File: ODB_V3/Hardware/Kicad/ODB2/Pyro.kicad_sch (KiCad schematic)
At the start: 51 parts, among them J1 Screw_Terminal_01x08, U11 SI5442DU-T1-GE3, U12 SI5442DU-T1-GE3, U2 LM339, U3 SI5442DU-T1-GE3, U8 SI5442DU-T1-GE3

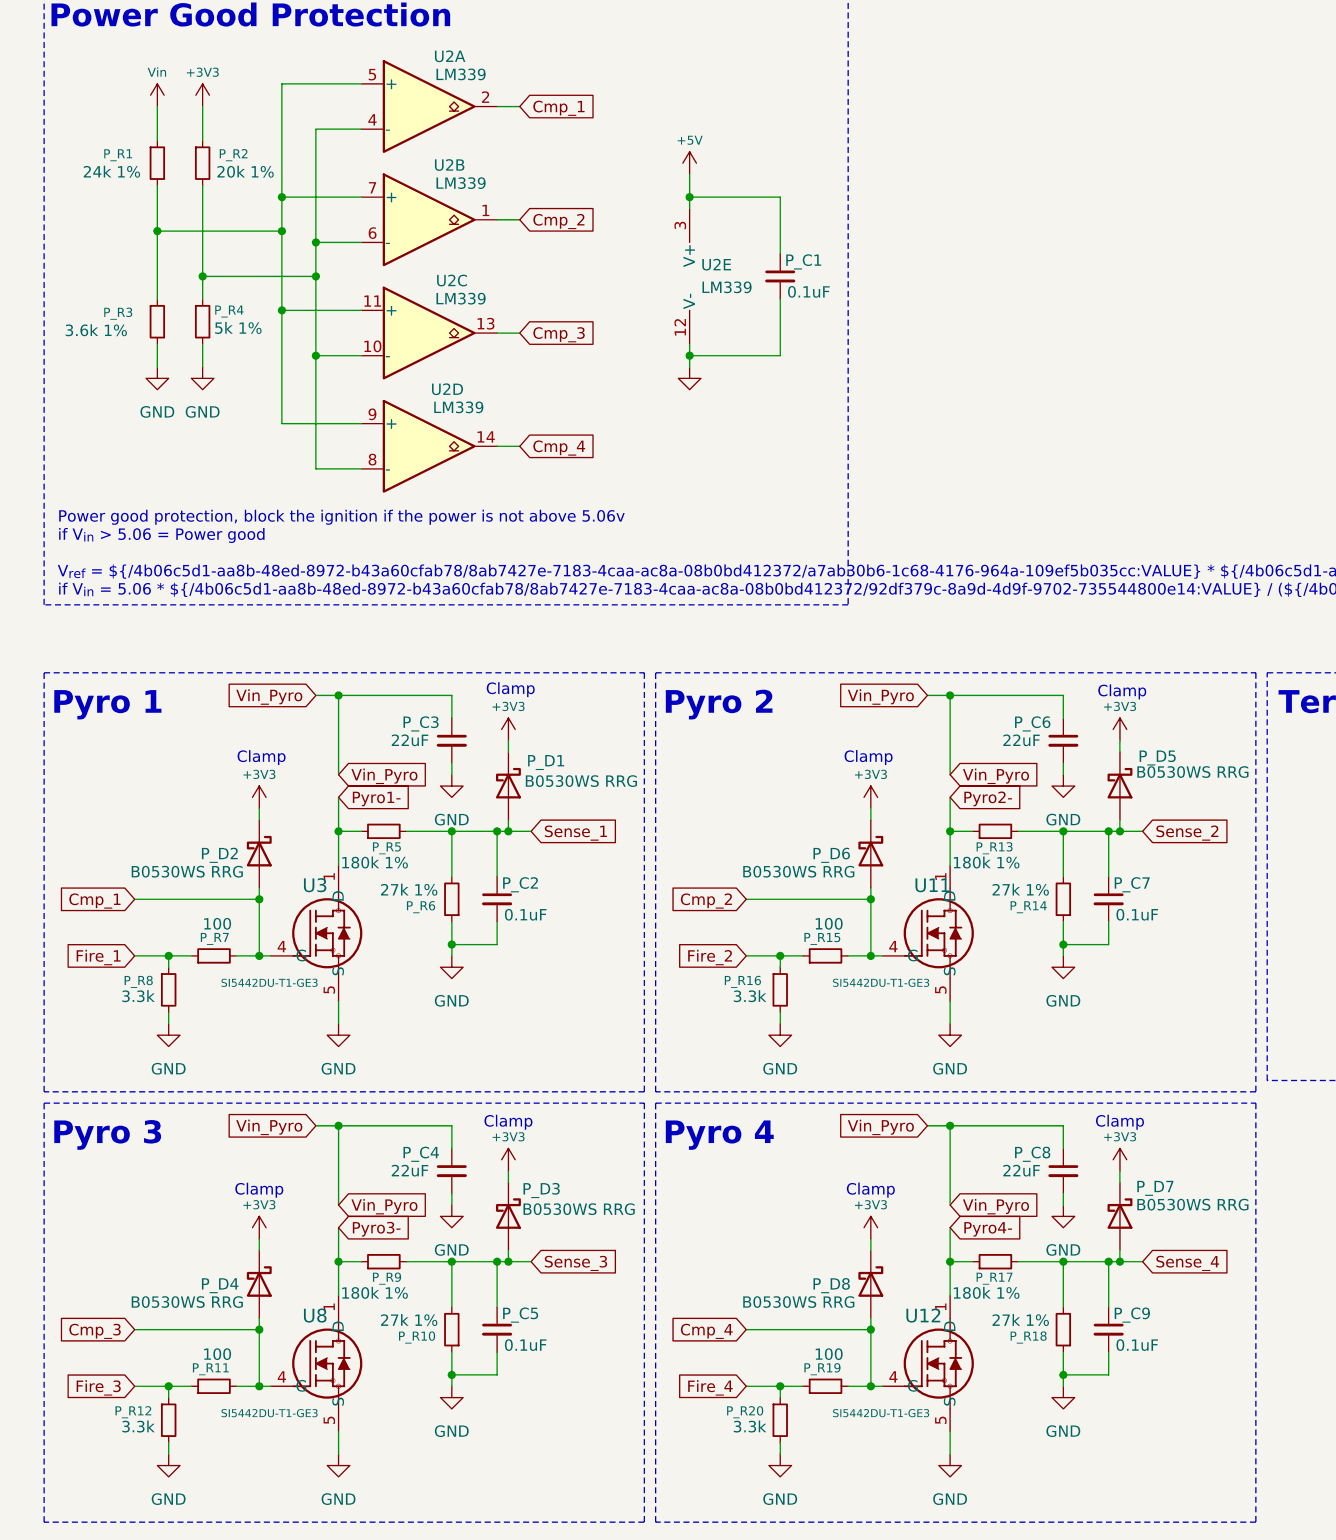
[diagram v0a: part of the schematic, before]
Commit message: wip : reduce BOM size
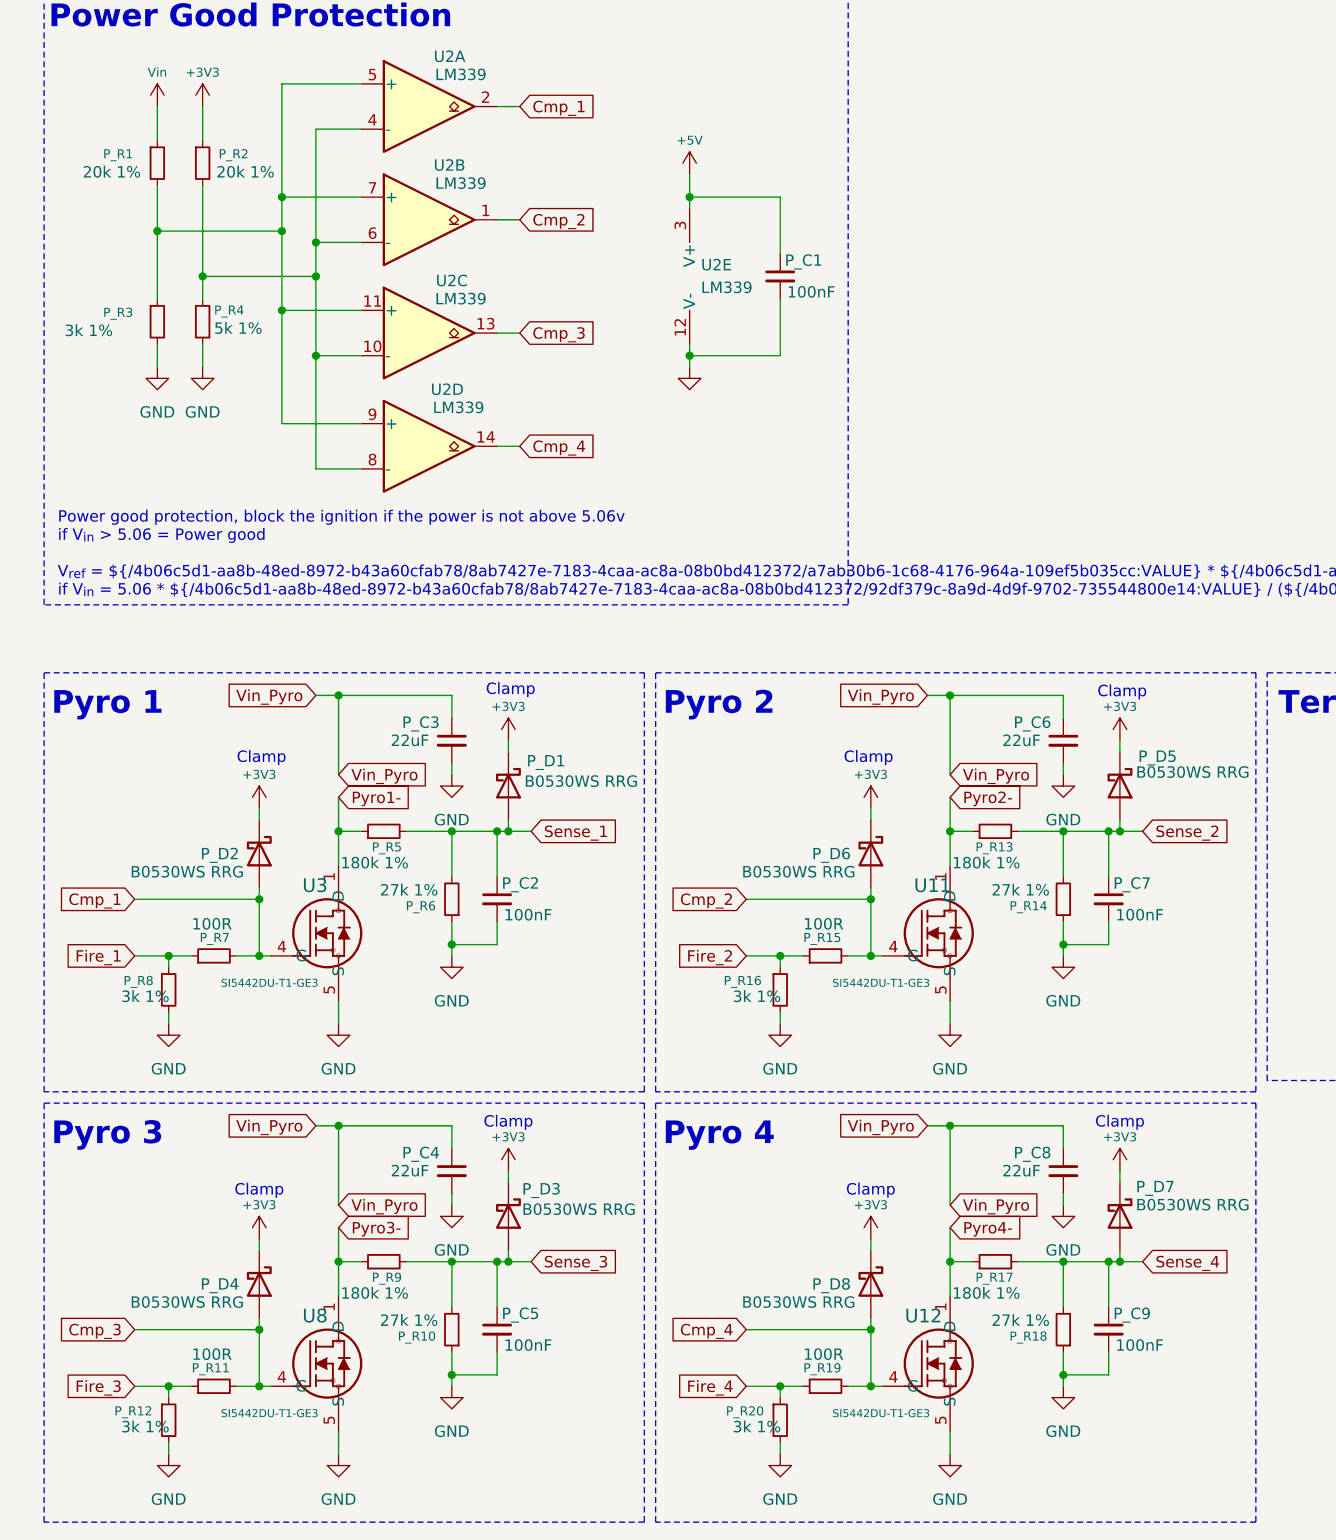
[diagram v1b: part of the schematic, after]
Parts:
- P_C1, P_C2, P_C5, P_C7, P_C9: value 0.1uF -> 100nF; footprint Capacitor_SMD:C_0603_1608Metric -> ODB:C_0402_1005Metric
- P_R1: value 24k 1% -> 20k 1%
- P_R11, P_R15, P_R19, P_R7: value 100 -> 100R
- P_R12, P_R16, P_R20, P_R8: value 3.3k -> 3k 1%
- P_R3: value 3.6k 1% -> 3k 1%
- Vin_C1: footprint Capacitor_SMD:C_0603_1608Metric -> ODB:C_0402_1005Metric
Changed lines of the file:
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@@
 			)
 		)
-		(property "Value" "3.3k"
+		(property "Value" "3k 1%"
 			(at 23.876 182.372 0)
 			(effects
@@
 			)
 		)
-		(property "Value" "100"
+		(property "Value" "100R"
 			(at 104.902 174.244 90)
 			(effects
@@
 			)
 		)
-		(property "Value" "0.1uF"
+		(property "Value" "100nF"
 			(at 66.802 173.228 0)
 			(effects
@@
 			)
 		)
-		(property "Footprint" "Capacitor_SMD:C_0603_1608Metric"
+		(property "Footprint" "ODB:C_0402_1005Metric"
 			(at 66.04 171.45 0)
 			(effects
@@
 			)
 		)
-		(property "Value" "0.1uF"
+		(property "Value" "100nF"
 			(at 135.382 124.968 0)
 			(effects
@@
 			)
 		)
-		(property "Footprint" "Capacitor_SMD:C_0603_1608Metric"
+		(property "Footprint" "ODB:C_0402_1005Metric"
 			(at 134.62 123.19 0)
 			(effects
@@
 			)
 		)
-		(property "Value" "100"
+		(property "Value" "100R"
 			(at 36.322 174.244 90)
 			(effects
@@
 			)
 		)
-		(property "Value" "24k 1%"
+		(property "Value" "20k 1%"
 			(at 19.558 41.656 0)
 			(effects
@@
 			)
 		)
-		(property "Footprint" "Capacitor_SMD:C_0603_1608Metric"
+		(property "Footprint" "ODB:C_0402_1005Metric"
 			(at 250.19 66.04 0)
 			(effects
@@
 			)
 		)
-		(property "Value" "100"
+		(property "Value" "100R"
 			(at 104.902 125.984 90)
 			(effects
@@
 			)
 		)
-		(property "Value" "3.6k 1%"
+		(property "Value" "3k 1%"
 			(at 17.526 59.436 0)
 			(effects
@@
 			)
 		)
-		(property "Value" "0.1uF"
+		(property "Value" "100nF"
 			(at 66.802 124.968 0)
 			(effects
@@
 			)
 		)
-		(property "Footprint" "Capacitor_SMD:C_0603_1608Metric"
+		(property "Footprint" "ODB:C_0402_1005Metric"
 			(at 66.04 123.19 0)
 			(effects
@@
 			)
 		)
-		(property "Value" "3.3k"
+		(property "Value" "3k 1%"
 			(at 92.456 182.372 0)
 			(effects
@@
 			)
 		)
-		(property "Value" "3.3k"
+		(property "Value" "3k 1%"
 			(at 23.876 134.112 0)
 			(effects
@@
 			)
 		)
-		(property "Value" "0.1uF"
+		(property "Value" "100nF"
 			(at 135.382 173.228 0)
 			(effects
@@
 			)
 		)
-		(property "Footprint" "Capacitor_SMD:C_0603_1608Metric"
+		(property "Footprint" "ODB:C_0402_1005Metric"
 			(at 134.62 171.45 0)
 			(effects
@@
 			)
 		)
-		(property "Value" "3.3k"
+		(property "Value" "3k 1%"
 			(at 92.456 134.112 0)
 			(effects
@@
 			)
 		)
-		(property "Value" "100"
+		(property "Value" "100R"
 			(at 36.322 125.984 90)
 			(effects
@@
 			)
 		)
-		(property "Value" "0.1uF"
+		(property "Value" "100nF"
 			(at 98.552 55.118 0)
 			(effects
@@
 			)
 		)
-		(property "Footprint" "Capacitor_SMD:C_0603_1608Metric"
+		(property "Footprint" "ODB:C_0402_1005Metric"
 			(at 97.79 53.34 0)
 			(effects

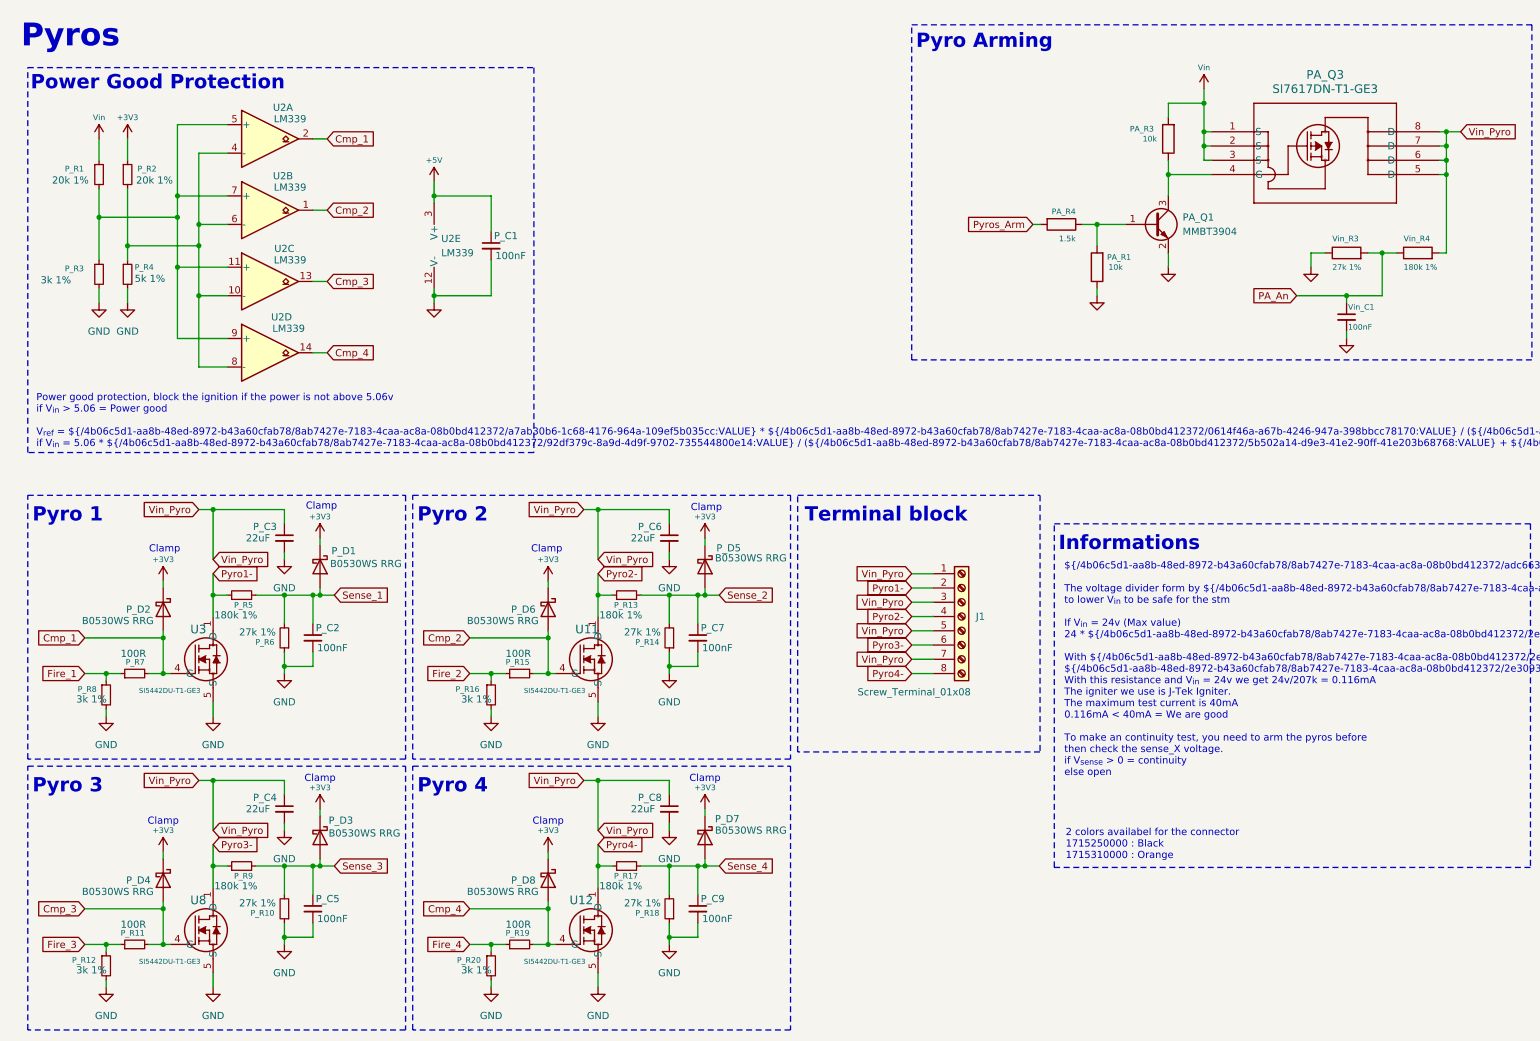
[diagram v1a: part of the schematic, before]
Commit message: wip : change REFDES to match manifacturing conventions
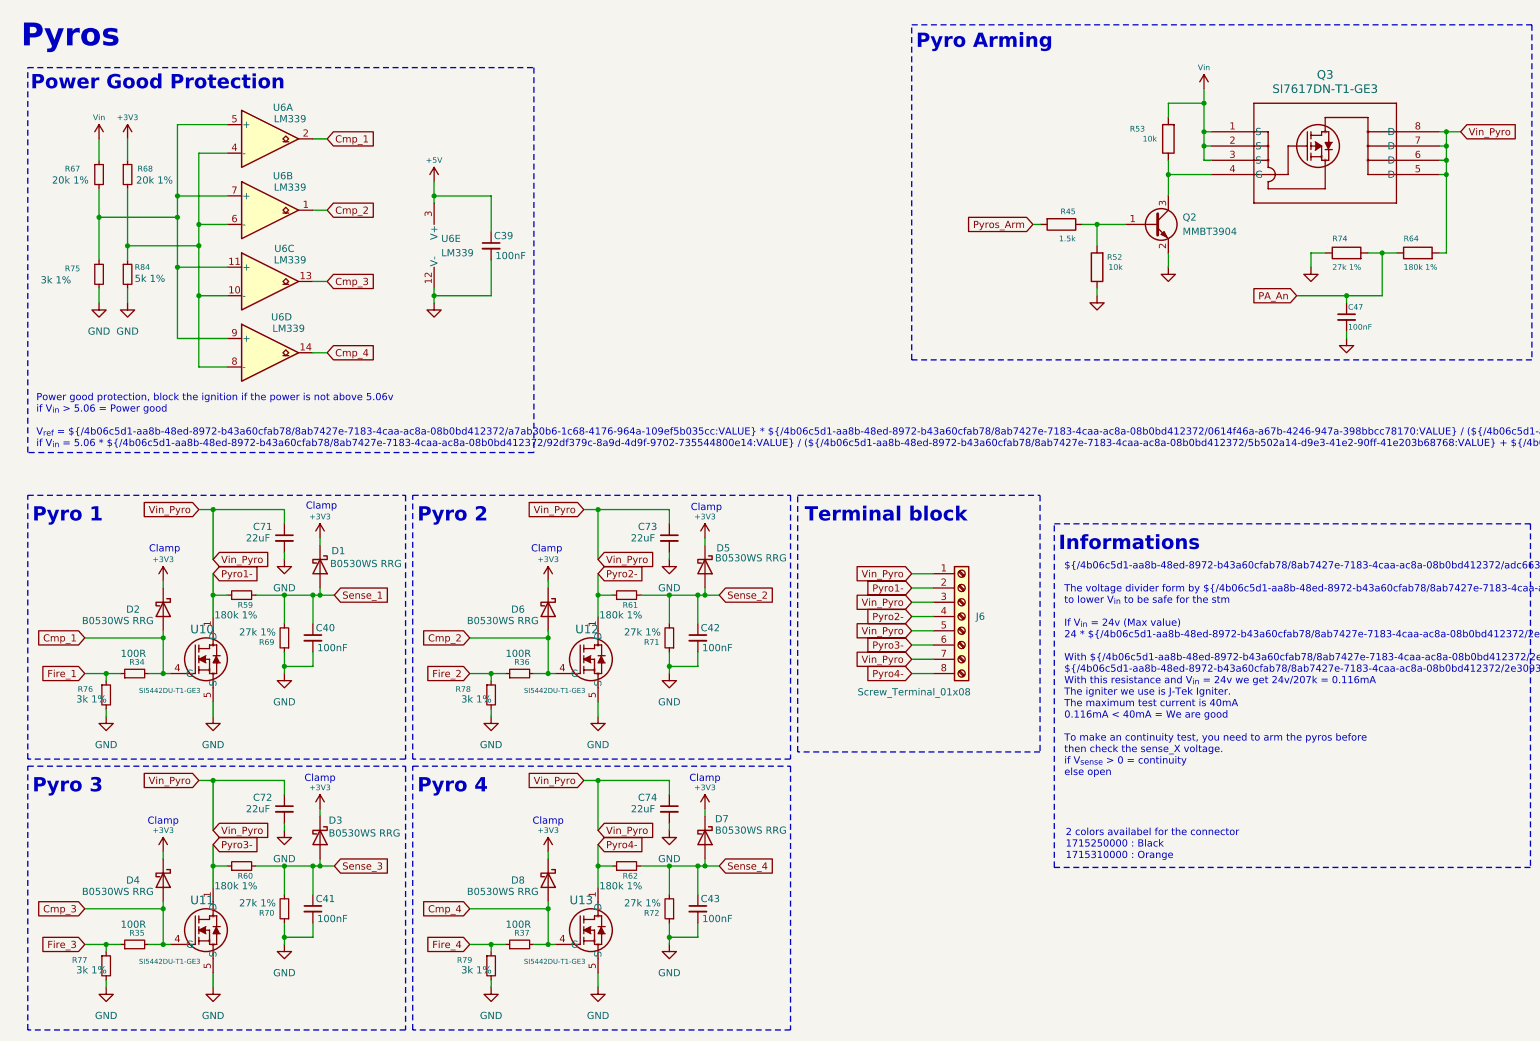
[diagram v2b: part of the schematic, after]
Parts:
- renumbered P_C1 to C39, P_C2 to C40, P_C5 to C41, P_C7 to C42, P_C9 to C43, Vin_C1 to C47, P_C3 to C71, P_C4 to C72, P_C6 to C73, P_C8 to C74, P_D1 to D1, P_D2 to D2, P_D3 to D3, P_D4 to D4, P_D5 to D5, P_D6 to D6, P_D7 to D7, P_D8 to D8, J1 to J6, PA_Q1 to Q2, PA_Q3 to Q3, P_R7 to R34, P_R11 to R35, P_R15 to R36, P_R19 to R37, PA_R4 to R45, PA_R1 to R52, PA_R3 to R53, P_R5 to R59, P_R9 to R60, P_R13 to R61, P_R17 to R62, Vin_R4 to R64, P_R1 to R67, P_R2 to R68, P_R6 to R69, P_R10 to R70, P_R14 to R71, P_R18 to R72, Vin_R3 to R74, P_R3 to R75, P_R8 to R76, P_R12 to R77, P_R16 to R78, P_R20 to R79, P_R4 to R84, U3 to U10, U8 to U11, U11 to U12, U12 to U13, U2 to U6

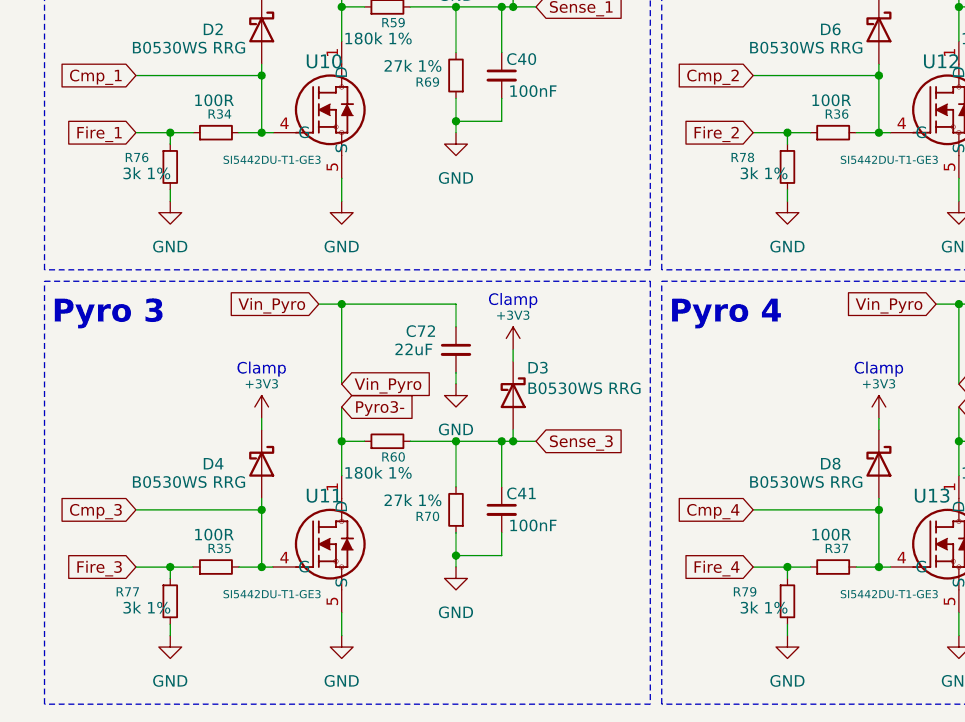
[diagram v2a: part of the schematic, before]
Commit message: fix: change 3k pulldown resistor in pyro to 5k
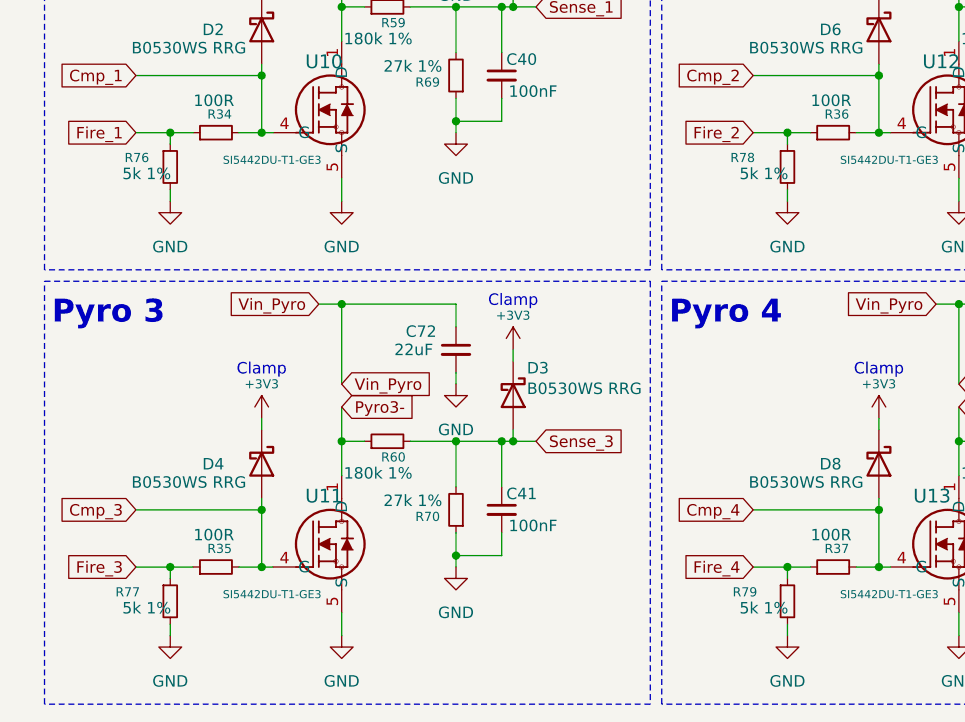
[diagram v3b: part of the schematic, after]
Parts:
- R76, R77, R78, R79: value 3k 1% -> 5k 1%
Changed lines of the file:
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@@
 			)
 		)
-		(property "Value" "3k 1%"
+		(property "Value" "5k 1%"
 			(at 23.876 182.372 0)
 			(effects
@@
 			)
 		)
-		(property "Value" "3k 1%"
+		(property "Value" "5k 1%"
 			(at 92.456 182.372 0)
 			(effects
@@
 			)
 		)
-		(property "Value" "3k 1%"
+		(property "Value" "5k 1%"
 			(at 23.876 134.112 0)
 			(effects
@@
 			)
 		)
-		(property "Value" "3k 1%"
+		(property "Value" "5k 1%"
 			(at 92.456 134.112 0)
 			(effects
